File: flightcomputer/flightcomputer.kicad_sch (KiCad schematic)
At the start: 65 parts, among them J1 Conn_Coaxial, J10 Conn_01x03, J11 Conn_01x03, J12 282837-2, J13 282837-2, J2 Conn_Coaxial, J3 Conn_Coaxial, J4 Conn_Coaxial, J5 Conn_01x24, J6 Conn_01x24, J7 Conn_01x01, J8 Conn_01x01, J9 Conn_01x02, M1 Motor_Servo, M2 Motor_Servo, Q1 MMBT3904, Q2 MMBT3904, Q3 SI4925DDY-T1-GE3, U1 MAX-M10S, U2 LIS2MDLTR, U3 BMI088, U4 MS5607-02BA, U5 MIC29302AWD-TR, U6 RFM95W-915S2, U7 Teensy4.1, U8 LD1117S50TR_SOT223

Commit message: all boards
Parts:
- removed C11, C7: 10uF, Capacitor_SMD:C_0603_1608Metric_Pad1.08x0.95mm_HandSolder, symbol Device:C
- removed C8: 22uF, Capacitor_SMD:C_0603_1608Metric_Pad1.08x0.95mm_HandSolder, symbol Device:C
- removed C9: 100nF, Capacitor_SMD:C_0603_1608Metric_Pad1.08x0.95mm_HandSolder, symbol Device:C
- removed J12, J13: 282837-2, HPRfootprints:TE_282837-2, symbol HPRsymbols:282837-2
- removed M1, M2: Motor_Servo, Connector_PinHeader_2.54mm:PinHeader_1x03_P2.54mm_Vertical, symbol Motor:Motor_Servo
- removed Q1, Q2: MMBT3904, Package_TO_SOT_SMD:SOT-23, symbol Transistor_BJT:MMBT3904
- removed Q3: SI4925DDY-T1-GE3, HPRfootprints:SOIC127P600X175-8N, symbol HPRsymbols:SI4925DDY-T1-GE3
- removed R3: 1.2k, Resistor_SMD:R_0603_1608Metric_Pad0.98x0.95mm_HandSolder, symbol Device:R
- removed R4: 4.7k, Resistor_SMD:R_0603_1608Metric_Pad0.98x0.95mm_HandSolder, symbol Device:R
- removed R5, R6: 1K, Resistor_SMD:R_0603_1608Metric_Pad0.98x0.95mm_HandSolder, symbol Device:R
- removed R7, R8: 10K, Resistor_SMD:R_0603_1608Metric_Pad0.98x0.95mm_HandSolder, symbol Device:R
- removed S1, S2: KMR221GLFS, HPRfootprints:SW_KMR221GLFS, symbol HPRsymbols:KMR221GLFS
- removed TP1, TP2: TestPoint, Connector_PinHeader_2.54mm:PinHeader_1x01_P2.54mm_Vertical, symbol Connector:TestPoint
- removed TP3, TP4, TP6, TP7: TestPoint, TestPoint:TestPoint_Pad_1.0x1.0mm, symbol Connector:TestPoint
- removed U5: MIC29302AWD-TR, HPRfootprints:TO-252-5_MCH, symbol HPRsymbols:MIC29302AWD-TR
- removed U8: LD1117S50TR_SOT223, Package_TO_SOT_SMD:SOT-223-3_TabPin2, symbol Regulator_Linear:LD1117S50TR_SOT223
- added J12: M20-6102045, RHDR40W66P254_2X20_5146X500X1105P, symbol HPRsymbols:M20-6102045
- C10, J1, J2, J3, J4, R1, R2, U1, U6: now fitted
- R10, R11, R9: value 150 -> 500
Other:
- note removed: "5V LDO Linear Regulator"
- note removed: "6V 3A LDO Linear Regulator"
- note removed: "Pyro Channels"
- note removed: "Servos"
- note removed: "Teensy 3.3V pin should be good enough"
- note removed: "Teensy ON/OFF Switch"
- note removed: "pyro sense?"
- moved on the sheet: BZ1

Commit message: no esp32, may add
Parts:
- removed J5, J6: Conn_01x24, Connector_Molex:Molex_SL_171971-0024_1x24_P2.54mm_Vertical, symbol Connector_Generic:Conn_01x24
- removed J7, J8: Conn_01x01, Connector_PinHeader_2.54mm:PinHeader_1x01_P2.54mm_Vertical, symbol Connector_Generic:Conn_01x01
- removed J9: Conn_01x02, Connector_JST:JST_PH_S2B-PH-K_1x02_P2.00mm_Horizontal, symbol Connector_Generic:Conn_01x02
- removed TP5: TestPoint, TestPoint:TestPoint_Pad_1.0x1.0mm, symbol Connector:TestPoint
- removed U6: RFM95W-915S2, RF_Module:HOPERF_RFM9XW_SMD, symbol RF_Module:RFM95W-915S2
- added C7, C8: 100nF, Capacitor_SMD:C_0402_1005Metric_Pad0.74x0.62mm_HandSolder, symbol Device:C
- added D4, D5, D6: LED, LED_SMD:LED_0603_1608Metric_Pad1.05x0.95mm_HandSolder, symbol Device:LED
- added J13: Conn_01x07, Connector_Molex:Molex_SL_171971-0007_1x07_P2.54mm_Vertical, symbol Connector_Generic:Conn_01x07
- added R12, R13, R8: 500, Resistor_SMD:R_0603_1608Metric_Pad0.98x0.95mm_HandSolder, symbol Device:R
- added R3, R4, R5, R6: 0, Resistor_SMD:R_0603_1608Metric_Pad0.98x0.95mm_HandSolder, symbol Device:R
- added TP1: TestPoint, Connector_Pin:Pin_D0.7mm_L6.5mm_W1.8mm_FlatFork, symbol Connector:TestPoint
- added U5: ESP32-S3-WROOM-1-N4, HPRfootprints:XCVR_ESP32-S3-WROOM-1-N4, symbol HPRsymbols:ESP32-S3-WROOM-1-N4
- added U8: LSM6DSO32TR, HPRfootprints:XDCR_LSM6DSO32TR, symbol HPRsymbols:LSM6DSO32TR
- added U9: RFM96W-433S2, HPRfootprints:MODULE_RFM96W-433S2, symbol HPRsymbols:RFM96W-433S2
- J12: footprint RHDR40W66P254_2X20_5146X500X1105P -> HPRfootprints:RHDR40W66P254_2X20_5146X500X1105P
- U7: now fitted
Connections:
- net GND: now also C7.2, C8.2, D4.1 (K), D5.1 (K), D6.1 (K), J13.5 (Pin_5), U8.2 (SDX), U8.3 (SCX), U8.6 (GND), U8.7 (GND__1), U9.1 (GND), U9.10 (GND), U9.8 (GND)
- net GPS_int: no longer U7.43 (21_A7_RX5_BCLK1)
- net GPS_reset: no longer U7.42 (20_A6_TX5_LRCLK1)
- net GPS_scl: no longer U7.41 (19_A5_SCL)
- net GPS_sda: no longer U7.40 (18_A4_SDA)
- net SENSE_miso: now also U8.1 (SDO/SA0)
- net SENSE_mosi: now also U8.14 (SDA)
- net SENSE_sck: now also U8.13 (SCL)
- net buzz_pwm: no longer U7.25 (33_MCLK2)
- net ldo_5v: no longer U7.48 (VIN)
- net radio_cs: now also R3.1, U9.5 (NSS); no longer U7.20 (28_RX7)
- net radio_dio0: now also U9.7 (DIO5); no longer U7.21 (29_TX7)
- net radio_dio1: now also U9.12 (DIO4); no longer U7.22 (30_CRX3)
- net radio_dio2: now also U9.11 (DIO3); no longer U7.23 (31_CTX3)
- net radio_dio3: now also U9.16 (DIO2)
- net radio_dio4: now also U9.15 (DIO1)
- net radio_dio5: now also U9.14 (DIO0); no longer U7.24 (32_OUT1B)
- net radio_miso: now also R5.1, U9.3 (MOSI); no longer U7.3 (1_TX1_CTX2_MISO1)
- net radio_mosi: now also R4.1, U9.2 (MISO); no longer U7.18 (26_A12_MOSI1)
- net radio_reset: now also U9.6 (RESET); no longer U7.2 (0_RX1_CRX2_CS1)
- net radio_sck: now also R6.1, U9.4 (SCK); no longer U7.19 (27_A13_SCK1)
- net teensy_3.3v: now also J13.6 (Pin_6), U9.13 (3.3V)
- net at U7.49 (VUSB): now also TP1.1
- net at J3.1 (In), J4.1 (In): now also U9.9 (ANT)
- net FREE7 renamed lsmimu_int
- net lsmimu_int: now also U8.9 (INT2)
- net FREE8 renamed lsmimu_cs
- net lsmimu_cs: now also U8.12 (CS)
- new net: C7.1, U8.5 (VDDIO)
- new net: C8.1, U8.8 (VDD)
- new net: D5.2 (A), R12.2
- new net: D4.2 (A), R8.2
- new net: D6.2 (A), R13.2
- new net 5V: U7.48 (VIN)
- new net LED4: R8.1
- new net LED5: R12.1
- new net LED6: R13.1
- new net sd_cs: J13.1 (Pin_1), R3.2
- new net sd_miso: J13.3 (Pin_3), R5.2
- new net sd_mosi: J13.2 (Pin_2), R4.2
- new net sd_sck: J13.4 (Pin_4), R6.2
- no-connect marks 11 -> 14
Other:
- note added: "(Also back up SPI Line)"
- note added: "Adafruit SPI Flash SD Card - XTSD 4 GB"
- note added: "Board-to-Board PC104 Connector - 0.6in between PCBs"
- note added: "Breakout Connector [Connect from bottom]"
- note added: "ESP32"
- note added: "ESP32 LEDs"
- note added: "RFM96W-433S2 LoRa Module"
- note added: "Teensy 4.1"
- note added: "Teensy LEDs"
- note added: "surface mount (passive) antenna connector (check footprint!)"
- note added: "ufl or SMA connections"
- note removed: "2S _P Battery"
- note removed: "LEDs"
- note removed: "RFM95W-915S2 LoRa Module"
- note removed: "surface mount antenna connector (check footprint!)"
- note removed: "what connector for battery?"
- moved on the sheet: BZ1, C1, C10, C2, C3, C4, C5, C6, D1, D2, D3, H1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

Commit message: gps and radio additions
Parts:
- added BT1: 2998TR, 2998TR:BAT_2998TR, symbol HPRlibrary:2998TR
- added C9: 1uF, Capacitor_SMD:C_0603_1608Metric_Pad1.08x0.95mm_HandSolder, symbol Device:C
- added D10, D7, D8, D9: ESD9B5.0ST5G, Diode_SMD:D_SOD-923, symbol Diode:ESD9B5.0ST5G
- added J14: Conn_01x04, Connector_PinHeader_2.54mm:PinHeader_1x04_P2.54mm_Vertical, symbol Connector_Generic:Conn_01x04
- added J5, J6, J7, J8: S4B-PH-K-S_LF__SN_, SHDRRA4W50P0X200_1X4_990X760X480P, symbol HPRlibrary:S4B-PH-K-S_LF__SN_
- added J9: Conn_01x05, Connector_PinHeader_2.54mm:PinHeader_1x05_P2.54mm_Vertical, symbol Connector_Generic:Conn_01x05
- added R14, R15, R16, R7: 0, Resistor_SMD:R_0603_1608Metric_Pad0.98x0.95mm_HandSolder, symbol Device:R
- added TP2, TP3: TestPoint, Connector_Pin:Pin_D0.7mm_L6.5mm_W1.8mm_FlatFork, symbol Connector:TestPoint
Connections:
- net GND: now also BT1.N, C9.2, D10.1 (A1), D7.1 (A1), D8.1 (A1), D9.1 (A1)
- net GPS_int: now also U7.43 (21_A7_RX5_BCLK1)
- net GPS_reset: now also U7.42 (20_A6_TX5_LRCLK1)
- net GPS_scl: now also U7.41 (19_A5_SCL)
- net GPS_sda: now also U7.40 (18_A4_SDA)
- net buzz_pwm: now also U7.25 (33_MCLK2)
- net radio_cs: now also U5.35 (IO42), U7.2 (0_RX1_CRX2_CS1)
- net radio_dio0: now also U5.26 (IO45)
- net radio_dio1: now also U5.16 (IO46)
- net radio_dio2: now also U5.24 (IO47)
- net radio_dio3: no longer U7.26 (34_RX8)
- net radio_dio4: no longer U7.27 (35_TX8)
- net radio_dio5: now also U5.25 (IO48)
- net radio_miso: now also U5.32 (IO39), U7.3 (1_TX1_CTX2_MISO1)
- net radio_mosi: now also U5.33 (IO40), U7.18 (26_A12_MOSI1)
- net radio_reset: now also U5.31 (IO38), U7.24 (32_OUT1B)
- net radio_sck: now also U5.34 (IO41), U7.19 (27_A13_SCK1)
- net sd_cs: now also U5.21 (IO13)
- net sd_miso: now also U5.8 (IO15)
- net sd_mosi: now also U5.22 (IO14)
- net sd_sck: now also U5.9 (IO16)
- net teensy_3.3v: no longer U1.14 (VCC_RF), U1.6 (V_BCKP)
- net at U1.2 (TXD): now also TP3.1
- net at U1.3 (RXD): now also TP2.1
- net teensy_onoff: no longer names the net of U7.54 (ON_OFF)
- new net: D7.2 (A2), J1.1 (In), R14.1
- new net: R14.2, R7.1, U1.11 (RF_IN)
- new net: D10.2 (A2), J4.1 (In), R15.1
- new net: R15.2, R16.2, U9.9 (ANT)
- new net: D9.2 (A2), J3.1 (In), R16.1
- new net: D8.2 (A2), J2.1 (In), R7.2
- new net gps_vbckp: BT1.P1, BT1.P2, C9.1, U1.6 (V_BCKP)
- no-connect marks 14 -> 13
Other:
- note added: "0 ohm resistor for antenna select (Make Y footprint) Can also use 100p capacitors (impedance = 1/2pifC)"
- note added: "100mA in-rush"
- note added: "Board-to-Board PC104 Connector 0.6in between PCBs"
- note added: "Breakout Connector"
- note added: "ESP32 [EXCLUDED FROM BOARD]"
- note added: "Utilize Teensy flash memory"
- note removed: "(Also back up SPI Line)"
- note removed: "Board-to-Board PC104 Connector - 0.6in between PCBs"
- note removed: "Breakout Connector [Connect from bottom]"
- note removed: "ESP32"
- moved on the sheet: BZ1, C1, C10, C2, C3, C4, C5, C6, C7, C8, D1, D2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

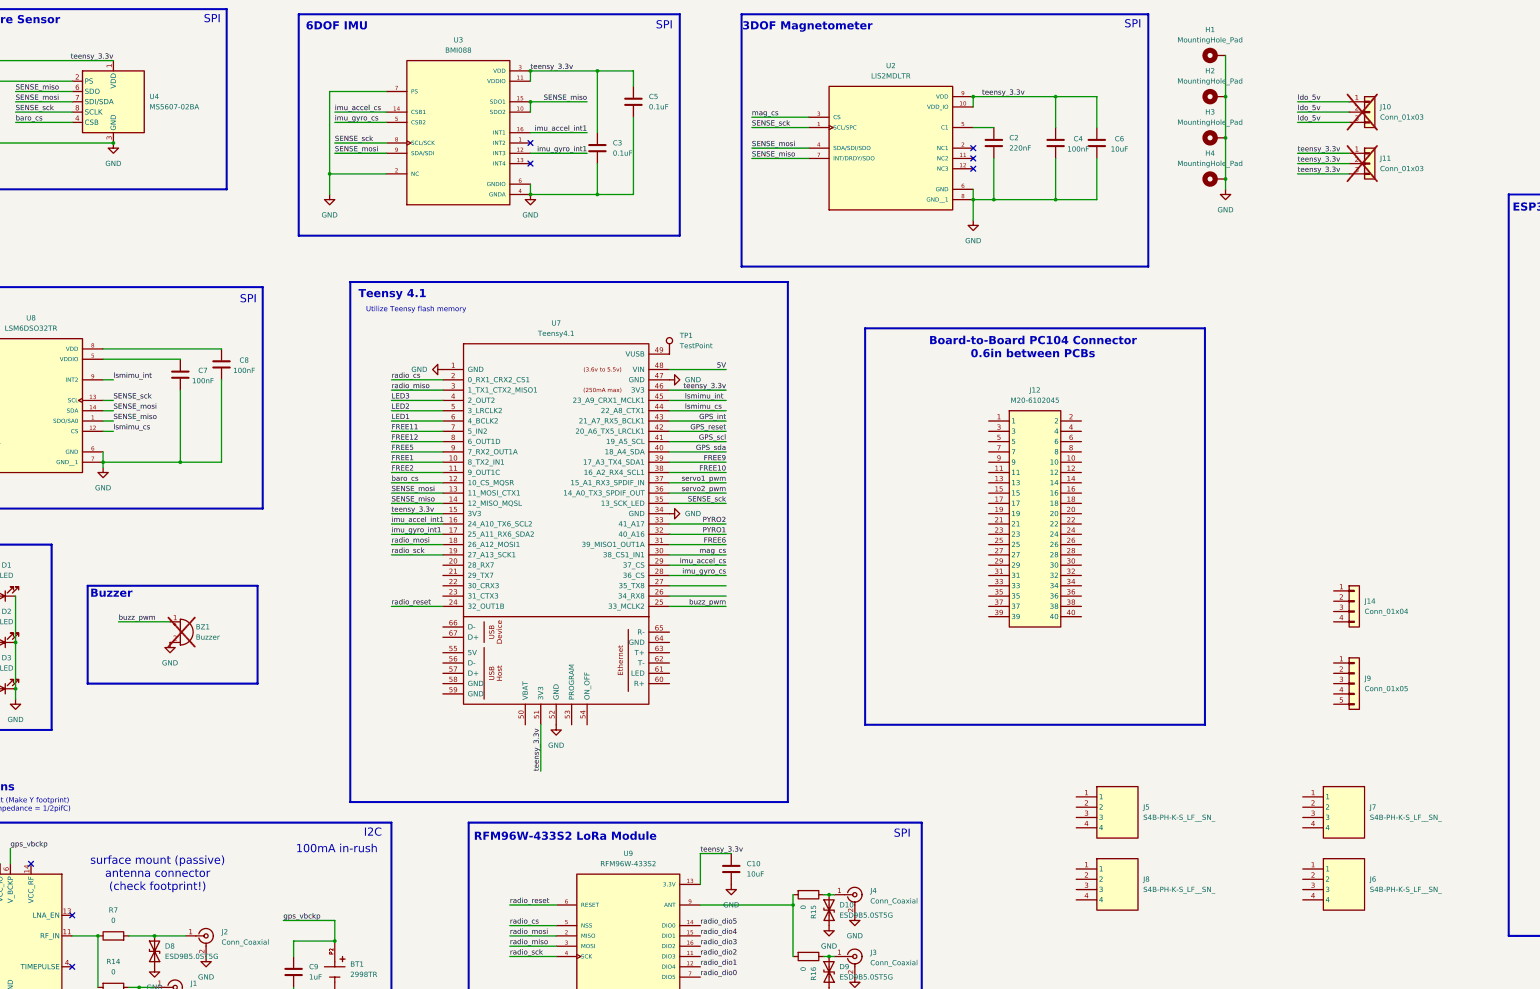
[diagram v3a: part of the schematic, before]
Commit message: added ports and test points
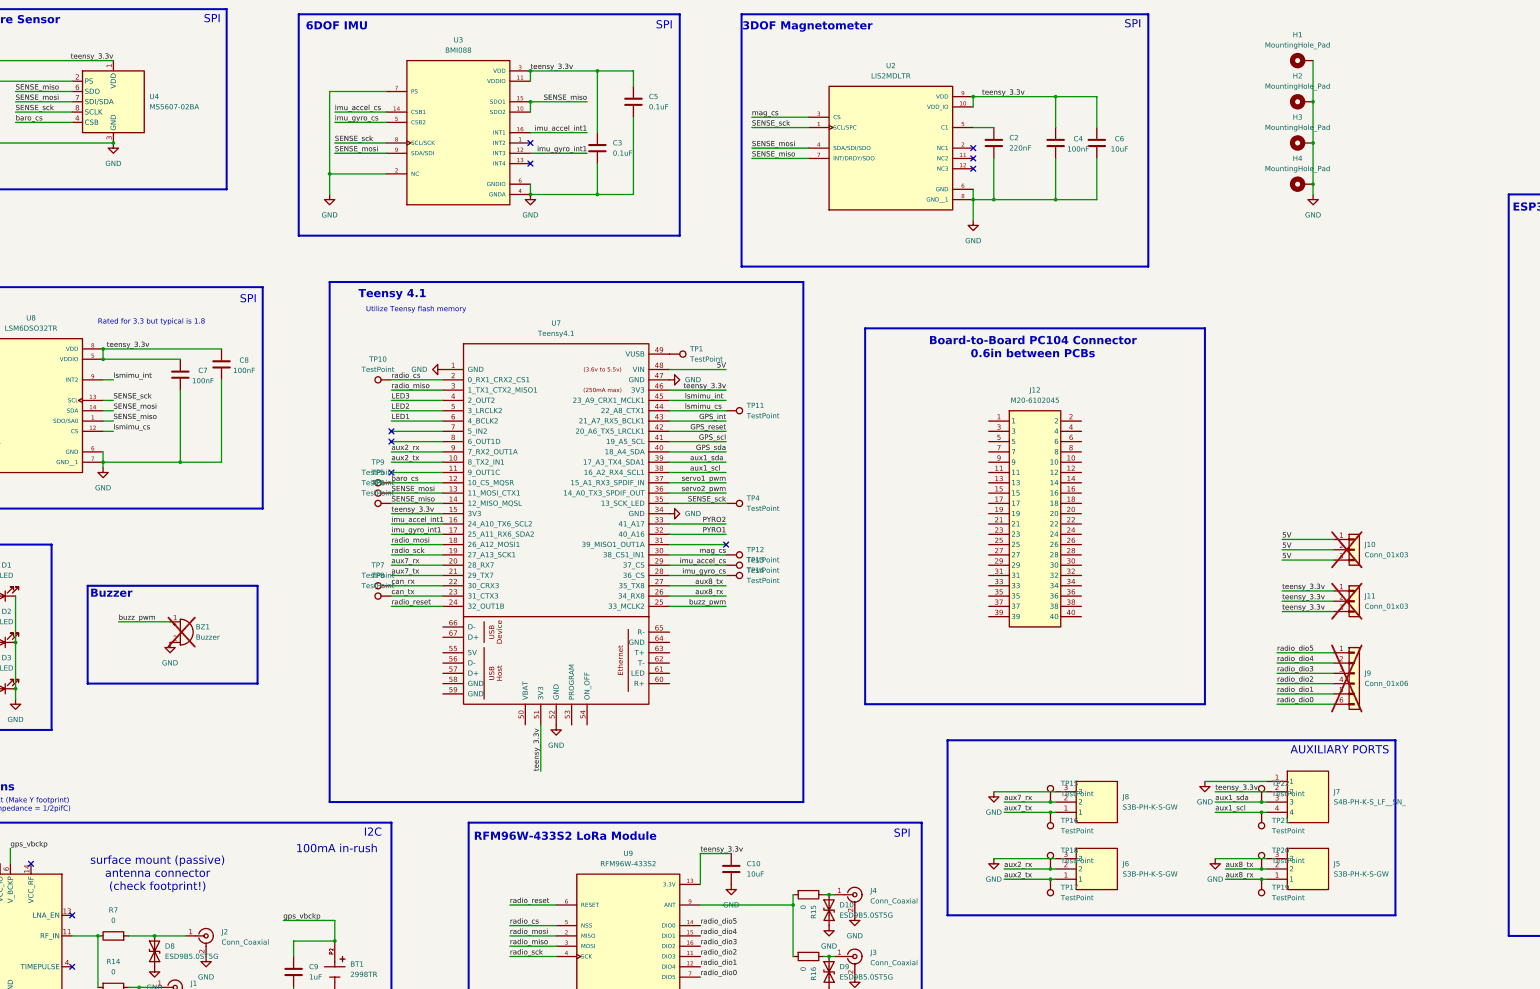
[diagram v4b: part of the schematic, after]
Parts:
- removed J14: Conn_01x04, Connector_PinHeader_2.54mm:PinHeader_1x04_P2.54mm_Vertical, symbol Connector_Generic:Conn_01x04
- removed J5, J6, J8: S4B-PH-K-S_LF__SN_, SHDRRA4W50P0X200_1X4_990X760X480P, symbol HPRlibrary:S4B-PH-K-S_LF__SN_
- removed J9: Conn_01x05, Connector_PinHeader_2.54mm:PinHeader_1x05_P2.54mm_Vertical, symbol Connector_Generic:Conn_01x05
- added J5, J6, J8: S3B-PH-K-S-GW, S3BPHKSGW, symbol HPRlibrary:S3B-PH-K-S-GW
- added J9: Conn_01x06, Connector_PinHeader_2.54mm:PinHeader_1x06_P2.54mm_Vertical, symbol Connector_Generic:Conn_01x06
- added TP10, TP11, TP12, TP13, TP14, TP15, TP16, TP17, TP18, TP19, TP20, TP21, TP22, TP4, TP5, TP6, TP7, TP8, TP9: TestPoint, Connector_PinHeader_2.54mm:PinHeader_1x01_P2.54mm_Vertical, symbol Connector:TestPoint
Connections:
- net FREE10 is gone; now on net aux1_scl: U7.38 (16_A2_RX4_SCL1)
- net FREE9 is gone; now on net aux1_sda: U7.39 (17_A3_TX4_SDA1)
- net ldo_5v is gone; now on net 5V: J10.1 (Pin_1), J10.2 (Pin_2), J10.3 (Pin_3)
- net GND: now also J7.1, J5.3, J6.3, J8.3
- net SENSE_miso: now also TP6.1
- net SENSE_mosi: now also TP5.1
- net SENSE_sck: now also TP4.1
- net baro_cs: now also TP9.1
- net imu_accel_cs: now also TP13.1
- net imu_gyro_cs: now also TP14.1
- net lsmimu_cs: now also TP11.1
- net mag_cs: now also TP12.1
- net radio_cs: now also TP10.1
- net radio_dio0: now also J9.6 (Pin_6)
- net radio_dio1: now also J9.5 (Pin_5)
- net radio_dio2: now also J9.4 (Pin_4)
- net radio_dio3: now also J9.3 (Pin_3)
- net radio_dio4: now also J9.2 (Pin_2)
- net radio_dio5: now also J9.1 (Pin_1)
- net teensy_3.3v: now also C7.1, C8.1, J7.2, U8.5 (VDDIO), U8.8 (VDD)
- net aux7_rx: now reaches U7.20 (28_RX7)
- net aux7_rx: now also J8.2, TP15.1
- net aux7_tx: now reaches U7.21 (29_TX7)
- net aux7_tx: now also J8.1, TP16.1
- net can_rx: now reaches U7.22 (30_CRX3)
- net can_rx: now also TP7.1
- net can_tx: now reaches U7.23 (31_CTX3)
- net can_tx: now also TP8.1
- net aux8_rx: now reaches U7.26 (34_RX8)
- net aux8_rx: now also J5.1, TP19.1
- net aux8_tx: now reaches U7.27 (35_TX8)
- net aux8_tx: now also J5.2, TP20.1
- net aux1_sda: now reaches J7.3
- net aux1_sda: now also TP22.1
- net aux1_scl: now reaches J7.4
- net aux1_scl: now also TP21.1
- net FREE1 renamed aux2_tx
- net aux2_tx: now also J6.1, TP17.1
- net FREE11: no longer names the net of U7.7 (5_IN2)
- net FREE12: no longer names the net of U7.8 (6_OUT1D)
- net FREE2: no longer names the net of U7.11 (9_OUT1C)
- net FREE5 renamed aux2_rx
- net aux2_rx: now also J6.2, TP18.1
- net FREE6: no longer names the net of U7.31 (39_MISO1_OUT1A)
- no-connect marks 13 -> 17
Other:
- note added: "AUXILIARY PORTS"
- note added: "Rated for 3.3 but typical is 1.8"
- moved on the sheet: H1, H2, H3, H4, J10, J11, J7, TP1

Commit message: placement
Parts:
- added R17: 0, Resistor_SMD:R_0603_1608Metric_Pad0.98x0.95mm_HandSolder, symbol Device:R
- added S1: EG1218, HPRlibrary:SW_EG1218, symbol HPRlibrary:EG1218
- BT1: footprint 2998TR:BAT_2998TR -> HPRlibrary:BAT_2998TR
- BZ1: now fitted
- C1, C2, C3, C4, C5, C6, C7, C8: footprint Capacitor_SMD:C_0402_1005Metric_Pad0.74x0.62mm_HandSolder -> Capacitor_SMD:C_0603_1608Metric_Pad1.08x0.95mm_HandSolder
- J12: footprint HPRfootprints:RHDR40W66P254_2X20_5146X500X1105P -> HPRlibrary:RHDR40W66P254_2X20_5146X500X1105P
- J5, J6, J8: footprint S3BPHKSGW -> HPRlibrary:S3BPHKSGW
- J7: footprint SHDRRA4W50P0X200_1X4_990X760X480P -> HPRlibrary:S4B-PH-K-S_LF__SN_
- TP1, TP2: footprint Connector_Pin:Pin_D0.7mm_L6.5mm_W1.8mm_FlatFork -> Connector_PinSocket_2.54mm:PinSocket_1x01_P2.54mm_Vertical
- TP3: footprint Connector_Pin:Pin_D0.7mm_L6.5mm_W1.8mm_FlatFork -> Connector_PinHeader_2.54mm:PinHeader_1x01_P2.54mm_Vertical
- U2: footprint HPRfootprints:PQFN50P200X200X70-12N -> HPRlibrary:PQFN50P200X200X70-12N
- U3: footprint HPRfootprints:PQFN50P450X300X100-16N -> HPRlibrary:PQFN50P450X300X100-16N
- U7: footprint HPRfootprints:Teensy41 -> HPRlibrary:Teensy41
- U8: footprint HPRfootprints:XDCR_LSM6DSO32TR -> HPRlibrary:XDCR_LSM6DSO32TR
- U9: footprint HPRfootprints:MODULE_RFM96W-433S2 -> HPRlibrary:MODULE_RFM96W-433S2
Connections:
- net radio_reset: now also TP1.1
- net teensy_3.3v: now also R17.2, S1.2; no longer R1.1, R2.1, U1.7 (VCC_IO), U1.8 (VCC)
- net at U7.49 (VUSB): no longer TP1.1
- new net gps_3.3v: R1.1, R17.1, R2.1, S1.3, U1.7 (VCC_IO), U1.8 (VCC)
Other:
- moved on the sheet: TP1
